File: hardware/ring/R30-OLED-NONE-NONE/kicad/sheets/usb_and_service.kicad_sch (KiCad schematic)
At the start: 4 parts, among them J1 USB-C

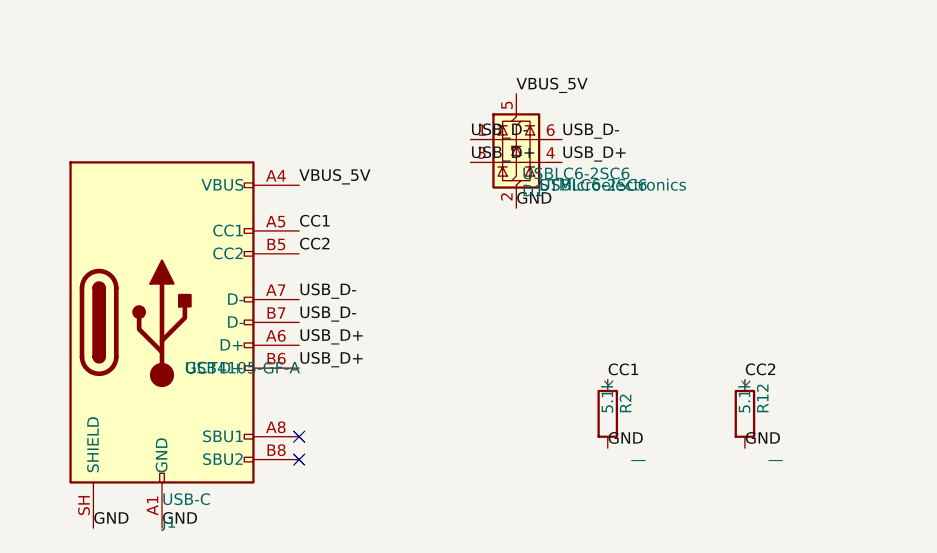
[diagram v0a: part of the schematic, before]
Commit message: feat(hardware): lock R30 sense and schematic baseline
Design disclosure: sensing mechanism PAW3204-class optical tracking; form factor R30-OLED-NONE-NONE fingertip ring, active 30-degree ring packet; intended use BLE HID pointing for accessibility; BOM estimate ~$5.30-9.45.

Record the accepted 2N7002 charge-gate path, R7-R11 sense/status values, current KiCad red baseline, and directly linked packet truth docs.
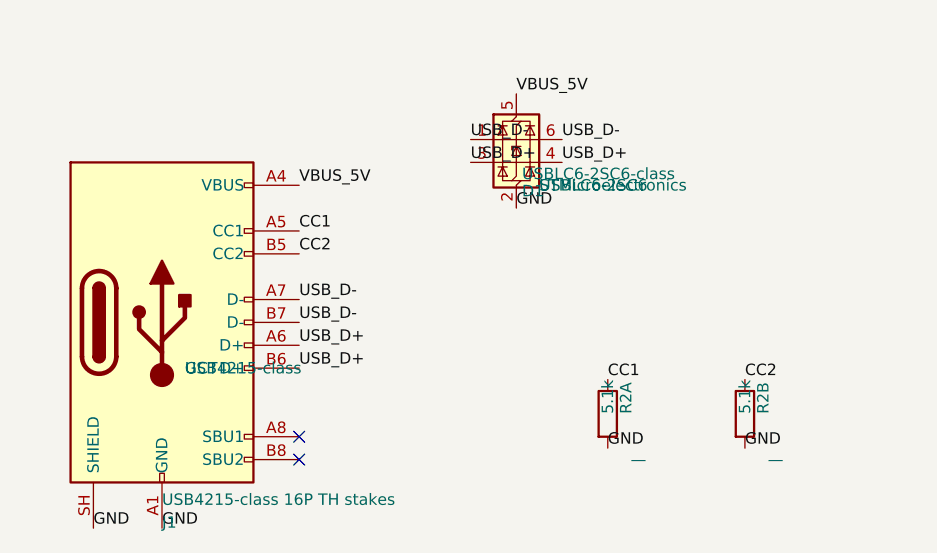
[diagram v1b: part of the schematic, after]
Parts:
- D1: value USBLC6-2SC6 -> USBLC6-2SC6-class
- J1: value USB-C -> USB4215-class 16P TH stakes; footprint Connector_USB:USB_C_Receptacle_GCT_USB4105-xx-A_16P_TopMnt_Horizontal -> PowerFinger_Ring:USB_C_Receptacle_GCT_USB4215_Class_16P_TH_Stakes; mfg_part_num USB4105-GF-A -> USB4215-class
- renumbered R2 to R2A, R12 to R2B
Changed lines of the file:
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@@
 			)
 		)
-		(property "Value" "USB-C"
+		(property "Value" "USB4215-class 16P TH stakes"
 			(at 90.17 99.695 0.0000)
 			(effects
@@
 			)
 		)
-		(property "Footprint" "Connector_USB:USB_C_Receptacle_GCT_USB4105-xx-A_16P_TopMnt_Horizontal"
+		(property "Footprint" "PowerFinger_Ring:USB_C_Receptacle_GCT_USB4215_Class_16P_TH_Stakes"
 			(at 93.98 80.01 0.0000)
 			(effects
@@
 			)
 		)
-		(property "mfg_part_num" "USB4105-GF-A"
+		(property "mfg_part_num" "USB4215-class"
 			(at 92.71 85.0899 0)
 			(effects
@@
 		(dnp no)
 		(fields_autoplaced no)
-		(property "Reference" "R2"
+		(property "Reference" "R2A"
 			(at 141.732 90.17 90)
 			(effects
@@
 			(project "simple_circuit"
 				(path "/5cdf6bc0-1d6d-4761-b5b2-853e85c36594"
-					(reference "R2")
+					(reference "R2A")
 					(unit 1)
 				)
@@
 		(dnp no)
 		(fields_autoplaced no)
-		(property "Reference" "R12"
+		(property "Reference" "R2B"
 			(at 156.972 90.17 90)
 			(effects
@@
 			(project "simple_circuit"
 				(path "/5cdf6bc0-1d6d-4761-b5b2-853e85c36594"
-					(reference "R12")
+					(reference "R2B")
 					(unit 1)
 				)
@@
 			)
 		)
-		(property "Value" "USBLC6-2SC6"
+		(property "Value" "USBLC6-2SC6-class"
 			(at 130.175 63.5 0.0000)
 			(effects

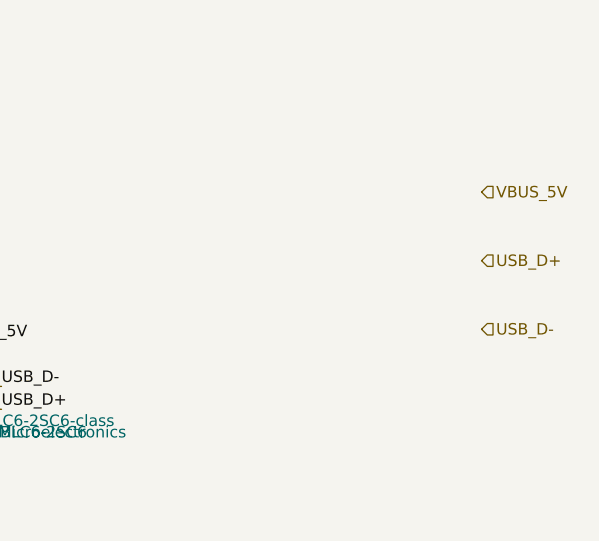
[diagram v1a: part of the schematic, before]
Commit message: fix(r30): clean schematic erc library baseline
Design disclosure: sensing mechanism PAW3204-class optical tracking; form factor R30-OLED-NONE-NONE fingertip ring, active 30-degree ring packet; intended use BLE HID pointing for accessibility; BOM estimate ~$5.30-9.45.

Materialize the project-local PowerFinger symbol and PowerFinger_Ring footprint libraries, wire sheet-interface labels, keep PAW3204 reset/motion local to sensor test pads, and update the verified KiCad snapshot to ERC=0, DRC=349, unconnected=41, parity=118.
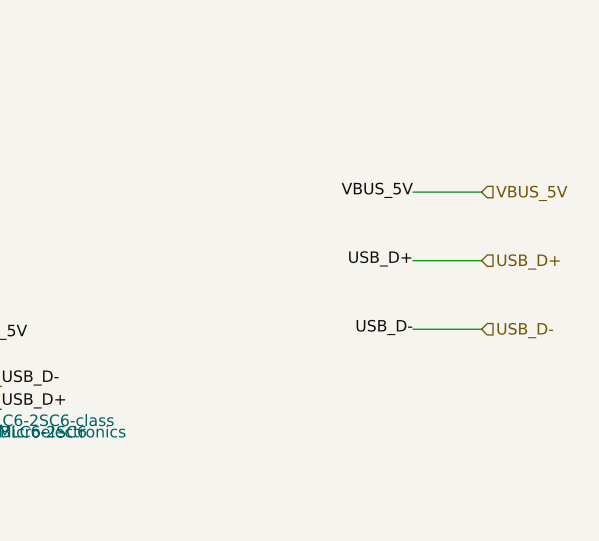
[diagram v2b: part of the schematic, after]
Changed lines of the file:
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@@
+		)
+	)
+	(wire
+		(pts
+			(xy 180.34 38.1) (xy 187.96 38.1)
+		)
+		(stroke (width 0) (type default) (color 0 0 0 0))
+	)
+	(label "VBUS_5V"
+		(at 180.34 38.1 180)
+		(effects
+			(font
+				(size 1.27 1.27)
+			)
+		)
+	)
+	(wire
+		(pts
+			(xy 180.34 45.72) (xy 187.96 45.72)
+		)
+		(stroke (width 0) (type default) (color 0 0 0 0))
+	)
+	(label "USB_D+"
+		(at 180.34 45.72 180)
+		(effects
+			(font
+				(size 1.27 1.27)
+			)
+		)
+	)
+	(wire
+		(pts
+			(xy 180.34 53.34) (xy 187.96 53.34)
+		)
+		(stroke (width 0) (type default) (color 0 0 0 0))
+	)
+	(label "USB_D-"
+		(at 180.34 53.34 180)
+		(effects
+			(font
+				(size 1.27 1.27)
+			)
 		)
 	)

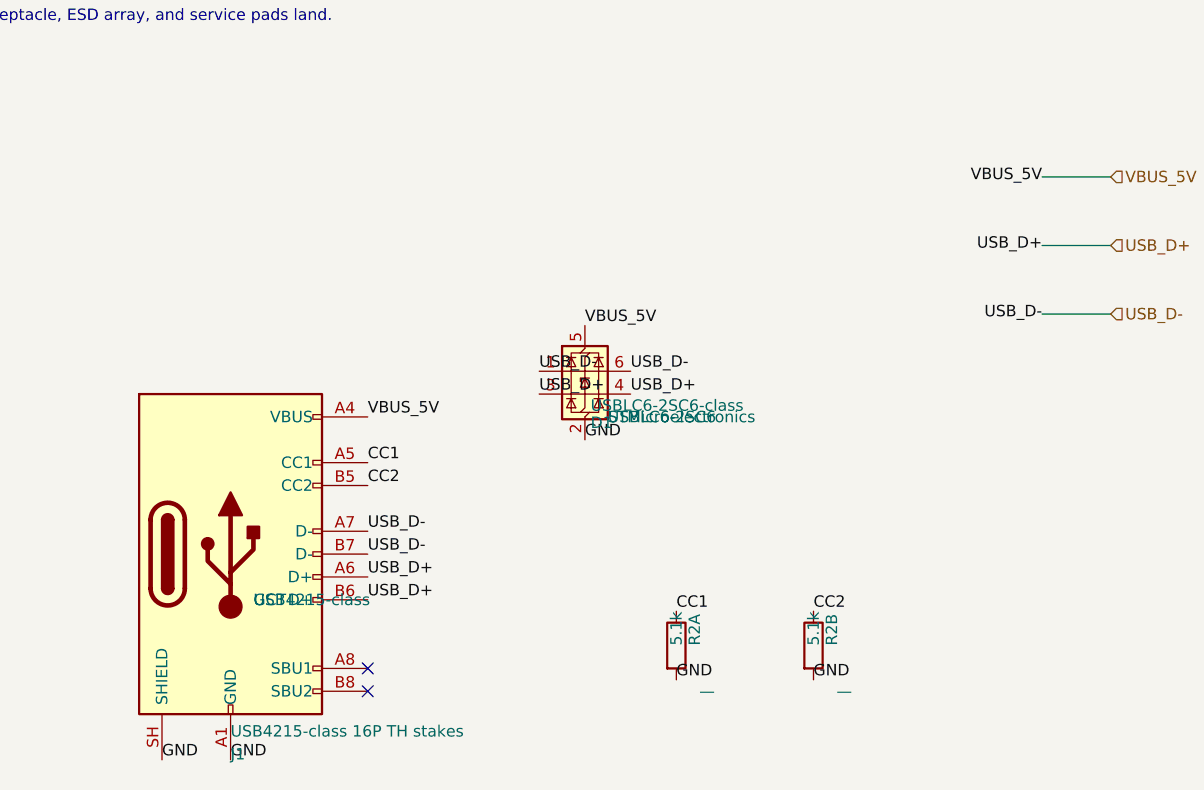
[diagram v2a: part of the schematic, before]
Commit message: fix(r30): reconcile schematic net parity
Sensing mechanism: PAW3204 optical surface tracking.

Form factor and angle: R30 30-degree ring, OLED/NONE/NONE active lane.

Intended use: accessibility-first BLE HID pointing first-board validation.

BOM estimate: active R30 prototype remains about .30-.45, target about .
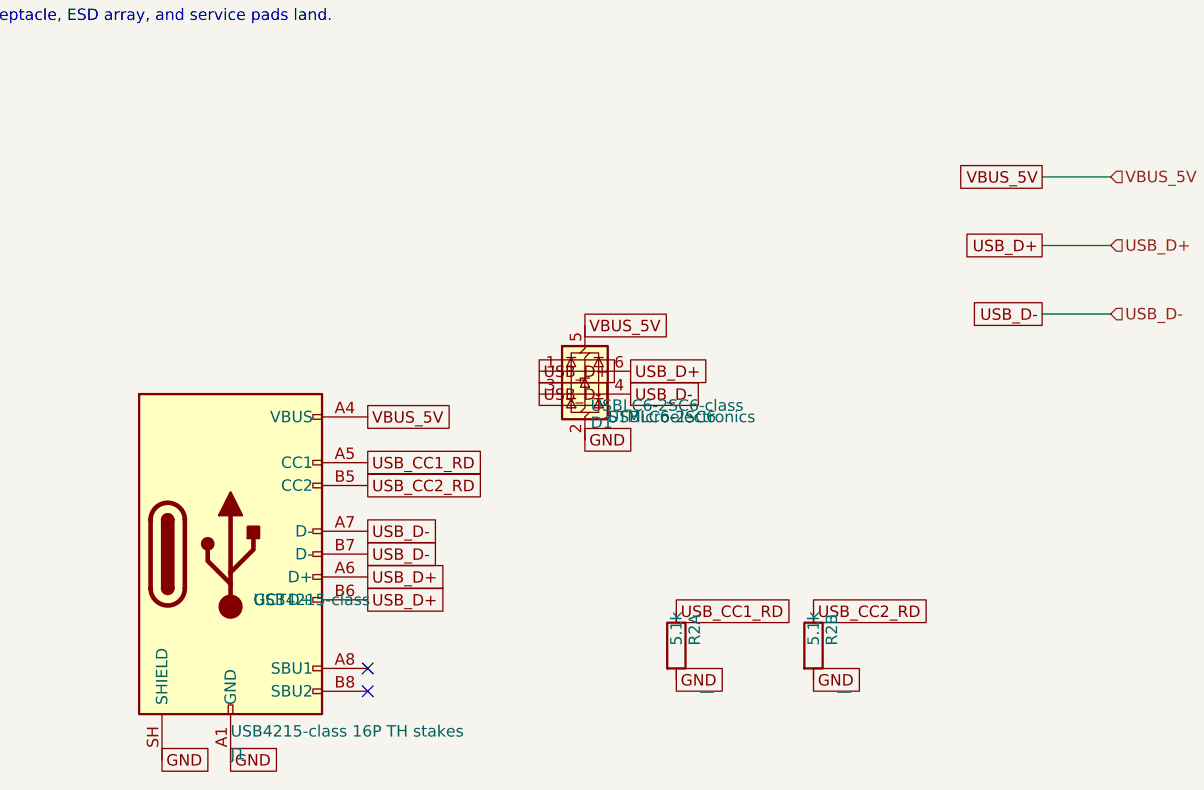
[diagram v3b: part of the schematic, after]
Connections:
- net USB_D+: now also D1.1 (I/O1), D1.6 (I/O1); no longer D1.3 (I/O2), D1.4 (I/O2)
- net USB_D-: now also D1.3 (I/O2), D1.4 (I/O2); no longer D1.1 (I/O1), D1.6 (I/O1)
- net CC1 renamed USB_CC1_RD
- net CC2 renamed USB_CC2_RD
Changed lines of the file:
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@@
 		)
 	)
-	(label "GND"
+	(global_label "GND"
+		(shape passive)
 		(at 90.17 102.87 0)
 		(effects
@@
 		)
 	)
-	(label "VBUS_5V"
+	(global_label "VBUS_5V"
+		(shape passive)
 		(at 105.41 64.77 0)
 		(effects
@@
 		)
 	)
-	(label "CC1"
+	(global_label "USB_CC1_RD"
+		(shape passive)
 		(at 105.41 69.85 0)
 		(effects
@@
 		)
 	)
-	(label "USB_D+"
+	(global_label "USB_D+"
+		(shape passive)
 		(at 105.41 82.55 0)
 		(effects
@@
 		)
 	)
-	(label "USB_D-"
+	(global_label "USB_D-"
+		(shape passive)
 		(at 105.41 77.47 0)
 		(effects
@@
 		)
 	)
-	(label "CC2"
+	(global_label "USB_CC2_RD"
+		(shape passive)
 		(at 105.41 72.39 0)
 		(effects
@@
 		)
 	)
-	(label "USB_D+"
+	(global_label "USB_D+"
+		(shape passive)
 		(at 105.41 85.09 0)
 		(effects
@@
 		)
 	)
-	(label "USB_D-"
+	(global_label "USB_D-"
+		(shape passive)
 		(at 105.41 80.01 0)
 		(effects
@@
 		)
 	)
-	(label "GND"
+	(global_label "GND"
+		(shape passive)
 		(at 82.55 102.87 0)
 		(effects
@@
 		)
 	)
-	(label "CC1"
+	(global_label "USB_CC1_RD"
+		(shape passive)
 		(at 139.7 86.36 0)
 		(effects
@@
 		)
 	)
-	(label "GND"
+	(global_label "GND"
+		(shape passive)
 		(at 139.7 93.98 0)
 		(effects
@@
 		)
 	)
-	(label "CC2"
+	(global_label "USB_CC2_RD"
+		(shape passive)
 		(at 154.94 86.36 0)
 		(effects
@@
 		)
 	)
-	(label "GND"
+	(global_label "GND"
+		(shape passive)
 		(at 154.94 93.98 0)
 		(effects
@@
 		)
 	)
-	(label "USB_D-"
+	(global_label "USB_D+"
+		(shape passive)
 		(at 124.46 59.69 0)
 		(effects
@@
 		)
 	)
-	(label "GND"
+	(global_label "GND"
+		(shape passive)
 		(at 129.54 67.31 0)
 		(effects
@@
 		)
 	)
-	(label "USB_D+"
+	(global_label "USB_D-"
+		(shape passive)
 		(at 124.46 62.23 0)
 		(effects
@@
 		)
 	)
-	(label "USB_D+"
+	(global_label "USB_D-"
+		(shape passive)
 		(at 134.62 62.23 0)
 		(effects
@@
 		)
 	)
-	(label "VBUS_5V"
+	(global_label "VBUS_5V"
+		(shape passive)
 		(at 129.54 54.61 0)
 		(effects
@@
 		)
 	)
-	(label "USB_D-"
+	(global_label "USB_D+"
+		(shape passive)
 		(at 134.62 59.69 0)
 		(effects
@@
 		(stroke (width 0) (type default) (color 0 0 0 0))
 	)
-	(label "VBUS_5V"
+	(global_label "VBUS_5V"
+		(shape passive)
 		(at 180.34 38.1 180)
 		(effects
@@
 		(stroke (width 0) (type default) (color 0 0 0 0))
 	)
-	(label "USB_D+"
+	(global_label "USB_D+"
+		(shape passive)
 		(at 180.34 45.72 180)
 		(effects
@@
 		(stroke (width 0) (type default) (color 0 0 0 0))
 	)
-	(label "USB_D-"
+	(global_label "USB_D-"
+		(shape passive)
 		(at 180.34 53.34 180)
 		(effects

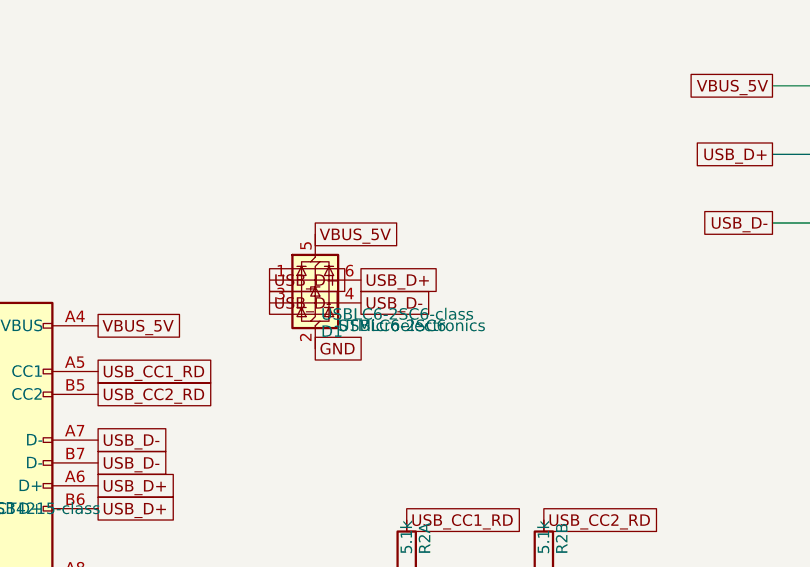
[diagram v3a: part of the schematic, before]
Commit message: fix(r30): replace d1 rail clamp esd
Sensing mechanism: PAW3204 optical surface tracking with rail-less dual USB data ESD protection on the service connector.

Form factor and angle: R30 30-degree ring, OLED/NONE/NONE active lane; D1 changes from USBLC6 SOT-23-6 rail clamp to TPD2E2U06DCK-class SC-70/SOT-323 data shunt.

Intended use: accessibility-first BLE HID pointing first-board validation with offline USB service/debug retained.

BOM estimate: active R30 prototype remains about .30-.45, target about ; D1 stays in the same about /bin/zsh.03-/bin/zsh.10 ESD protection class.
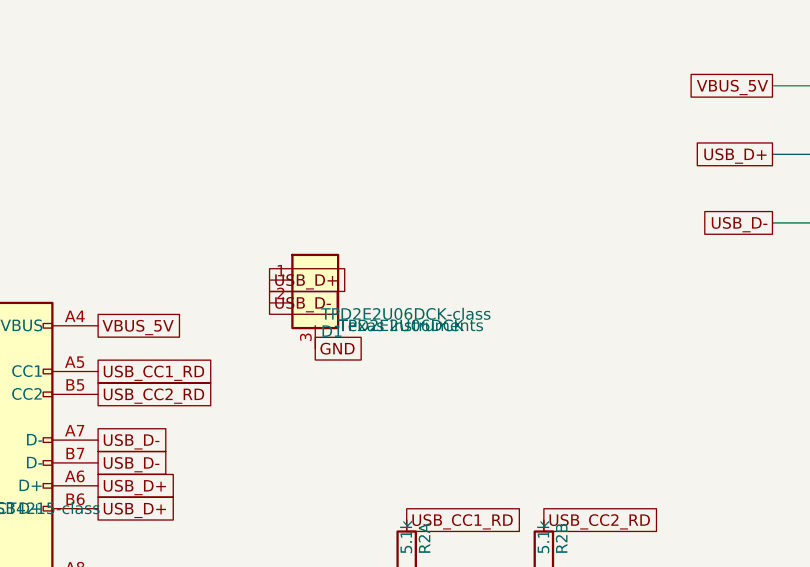
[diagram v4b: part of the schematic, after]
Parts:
- D1: value USBLC6-2SC6-class -> TPD2E2U06DCK-class; footprint Package_TO_SOT_SMD:SOT-23-6 -> Package_TO_SOT_SMD:SOT-323_SC-70; symbol Power_Protection:USBLC6-2SC6 -> PowerFinger:TPD2E2U06DCK_FirstBoard; manufacturer STMicroelectronics -> Texas Instruments; mfg_part_num USBLC6-2SC6 -> TPD2E2U06DCK
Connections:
- net GND: now also D1.3 (GND); no longer D1.2 (GND)
- net USB_D+: no longer D1.6 (I/O1)
- net USB_D-: now also D1.2 (IO2); no longer D1.3 (I/O2), D1.4 (I/O2)
- net VBUS_5V: no longer D1.5 (VBUS)
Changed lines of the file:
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@@
 	(generator_version "0.1")
 	(paper "A4")
-	(symbol
-		(lib_id "Connector:USB_C_Receptacle_USB2.0_16P")
+		(symbol
+			(lib_id "Connector:USB_C_Receptacle_USB2.0_16P")
 		(at 90.17 80.01 0)
 		(unit 1)
@@
 		)
 	)
-	(symbol
-		(lib_id "Power_Protection:USBLC6-2SC6")
-		(at 129.54 59.69 0)
+		(symbol
+			(lib_id "PowerFinger:TPD2E2U06DCK_FirstBoard")
+			(at 129.54 59.69 0)
 		(unit 1)
 		(exclude_from_sim no)
@@
 			)
 		)
-		(property "Value" "USBLC6-2SC6-class"
-			(at 130.175 63.5 0.0000)
-			(effects
-				(font
-					(size 1.27 1.27)
-				)
-				(justify left)
-			)
-		)
-		(property "Footprint" "Package_TO_SOT_SMD:SOT-23-6"
-			(at 130.81 53.34 0.0000)
+			(property "Value" "TPD2E2U06DCK-class"
+				(at 130.175 63.5 0.0000)
+			(effects
+				(font
+					(size 1.27 1.27)
+				)
+				(justify left)
+			)
+		)
+			(property "Footprint" "Package_TO_SOT_SMD:SOT-323_SC-70"
+				(at 130.81 53.34 0.0000)
 			(effects
 				(font
@@
 			)
 		)
-		(property "mfg_part_num" "USBLC6-2SC6"
-			(at 132.08 64.7699 0)
-			(effects
-				(font
-					(size 1.27 1.27)
-				)
-				(justify left)
-			)
-		)
-		(property "manufacturer" "STMicroelectronics"
-			(at 132.08 64.7699 0)
+			(property "mfg_part_num" "TPD2E2U06DCK"
+				(at 132.08 64.7699 0)
+			(effects
+				(font
+					(size 1.27 1.27)
+				)
+				(justify left)
+			)
+		)
+			(property "manufacturer" "Texas Instruments"
+				(at 132.08 64.7699 0)
 			(effects
 				(font
@@
 		(pin "3"
 		)
-		(pin "4"
-		)
-		(pin "5"
-		)
-		(pin "6"
-		)
-		(instances
+			(instances
 			(project "simple_circuit"
 				(path "/5cdf6bc0-1d6d-4761-b5b2-853e85c36594"
@@
 		)
 	)
-	(global_label "USB_D+"
-		(shape passive)
-		(at 124.46 59.69 0)
-		(effects
-			(font
-				(size 1.27 1.27)
-			)
-			(justify left bottom)
-		)
-	)
-	(global_label "GND"
-		(shape passive)
-		(at 129.54 67.31 0)
-		(effects
-			(font
-				(size 1.27 1.27)
-			)
-			(justify left bottom)
-		)
-	)
-	(global_label "USB_D-"
-		(shape passive)
-		(at 124.46 62.23 0)
-		(effects
-			(font
-				(size 1.27 1.27)
-			)
-			(justify left bottom)
-		)
-	)
-	(global_label "USB_D-"
-		(shape passive)
-		(at 134.62 62.23 0)
-		(effects
-			(font
-				(size 1.27 1.27)
-			)
-			(justify left bottom)
-		)
-	)
-	(global_label "VBUS_5V"
-		(shape passive)
-		(at 129.54 54.61 0)
-		(effects
-			(font
-				(size 1.27 1.27)
-			)
-			(justify left bottom)
-		)
-	)
-	(global_label "USB_D+"
-		(shape passive)
-		(at 134.62 59.69 0)
-		(effects
-			(font
+		(global_label "USB_D+"
+			(shape passive)
+			(at 124.46 59.69 0)
+		(effects
+			(font
+				(size 1.27 1.27)
+			)
+			(justify left bottom)
+		)
+	)
+		(global_label "GND"
+			(shape passive)
+			(at 129.54 67.31 0)
+		(effects
+			(font
+				(size 1.27 1.27)
+			)
+			(justify left bottom)
+		)
+	)
+		(global_label "USB_D-"
+			(shape passive)
+			(at 124.46 62.23 0)
+		(effects
+			(font
